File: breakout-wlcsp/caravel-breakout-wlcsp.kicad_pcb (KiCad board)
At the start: 2 copper layers, 45 x 52.5 mm, 43 parts, among them CON1 REF-182665-01, CON2 REF-182665-01, CON3 73251-1352, U1 Caravel

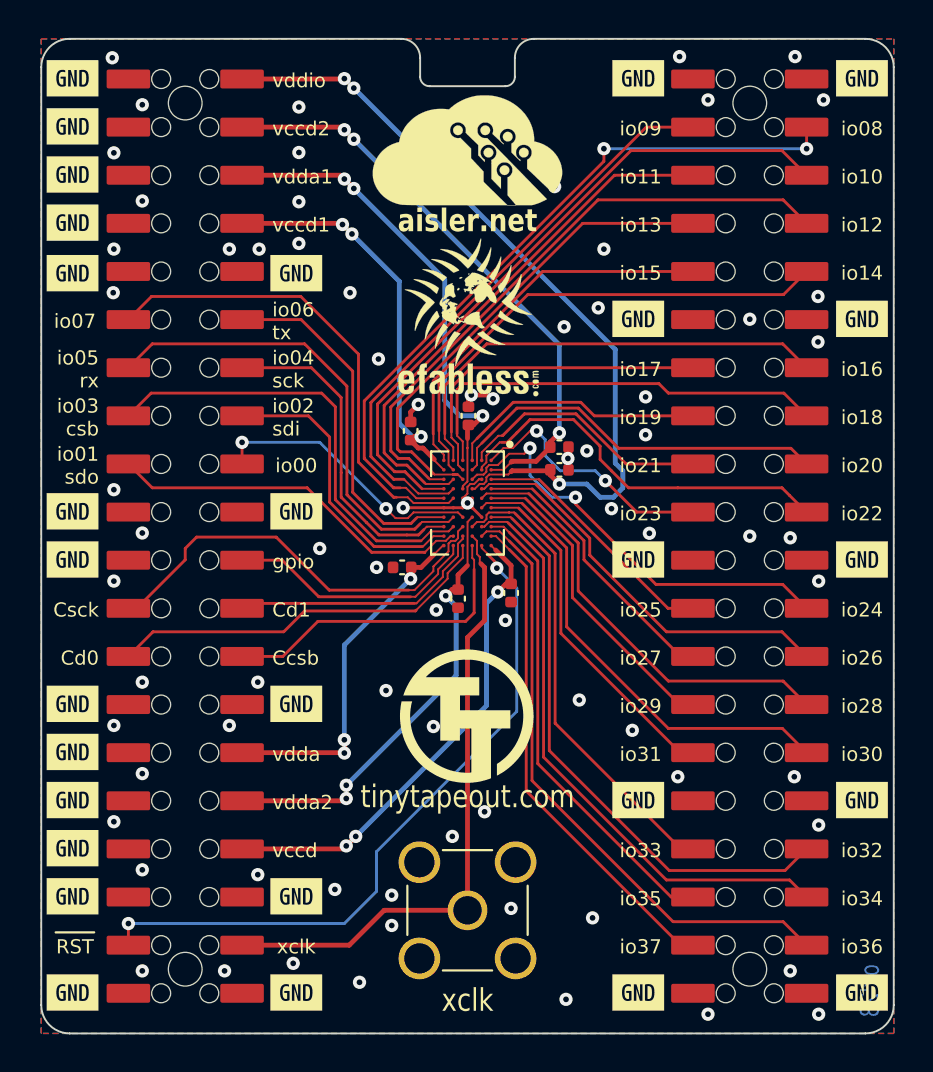
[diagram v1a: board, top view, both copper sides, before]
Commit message: Added fids and patch over-reliance on gnd fill for conn DRC fails
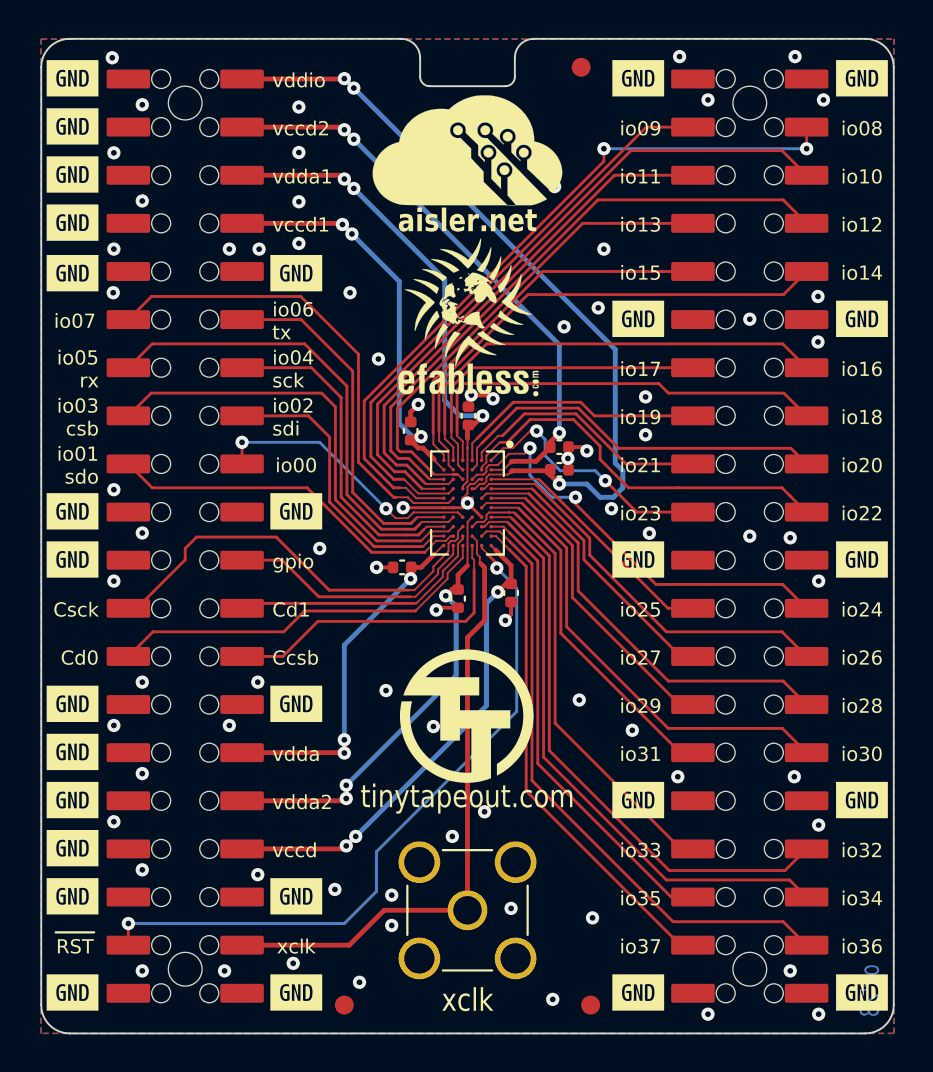
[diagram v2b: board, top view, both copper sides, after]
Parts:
- added FID1: Fiducial, Fiducial:Fiducial_1mm_Mask2mm, F.Cu at (66.2, 69.0)
- added FID2: Fiducial, Fiducial:Fiducial_1mm_Mask2mm, F.Cu at (79.2, 69.0)
- added FID3: Fiducial, Fiducial:Fiducial_1mm_Mask2mm, F.Cu at (78.7, 19.5)
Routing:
- net GND: track 9.89 -> 14.7 mm

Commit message: aisler requested mods
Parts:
- CON1, CON2: footprint ok-connectors:REF-182665-01 -> BreakoutCommon:REF-182665-01
